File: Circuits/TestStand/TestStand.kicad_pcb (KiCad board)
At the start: 2 copper layers, 105 x 142.5 mm, 109 parts, among them IC1 STP85NF55, J1 2601-1107, J10 Screw_Terminal_01x03, J11 Screw_Terminal_01x03, J12 Screw_Terminal_01x03, J13 Screw_Terminal_01x03, J14 CONN4_2606-1104/010-000_WAG, J15 Conn_Coaxial, J18 2601-1107, J2 2601-1107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

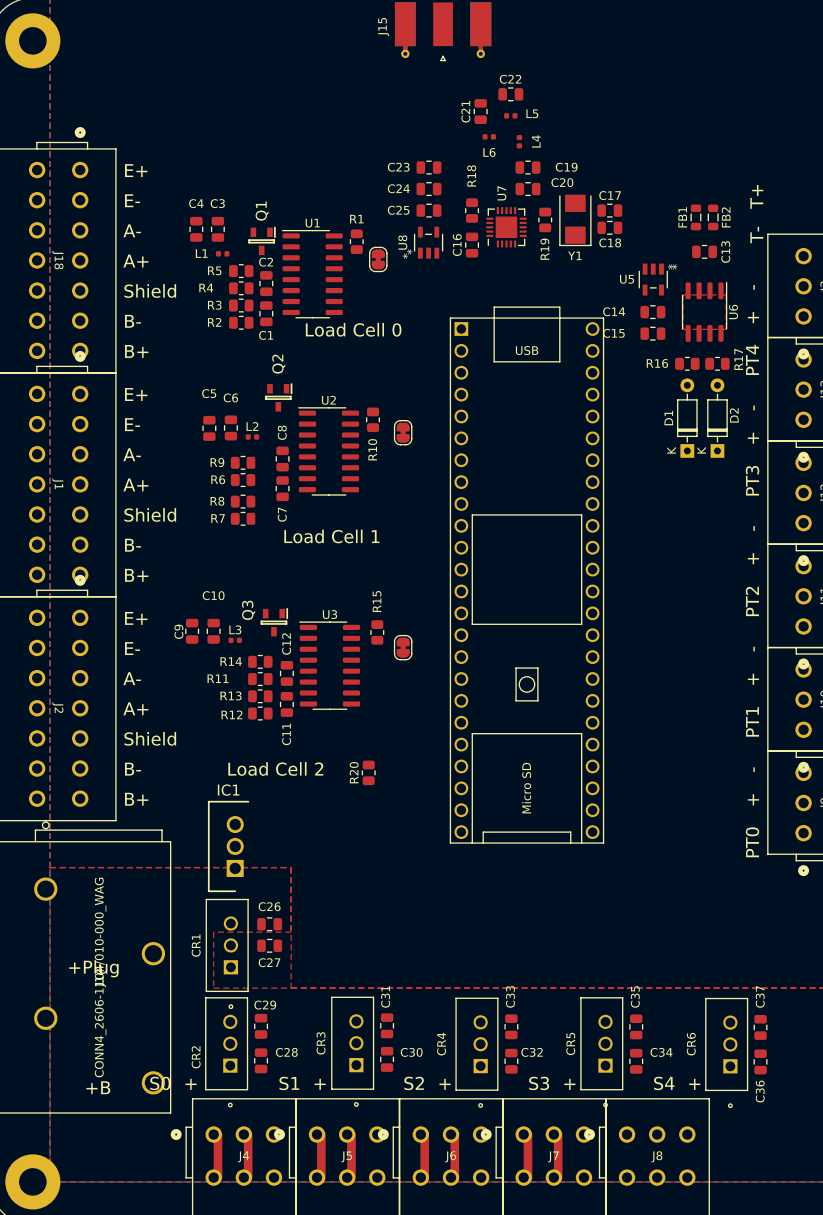
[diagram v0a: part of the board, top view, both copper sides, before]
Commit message: fixed 3d models, arranged nicely
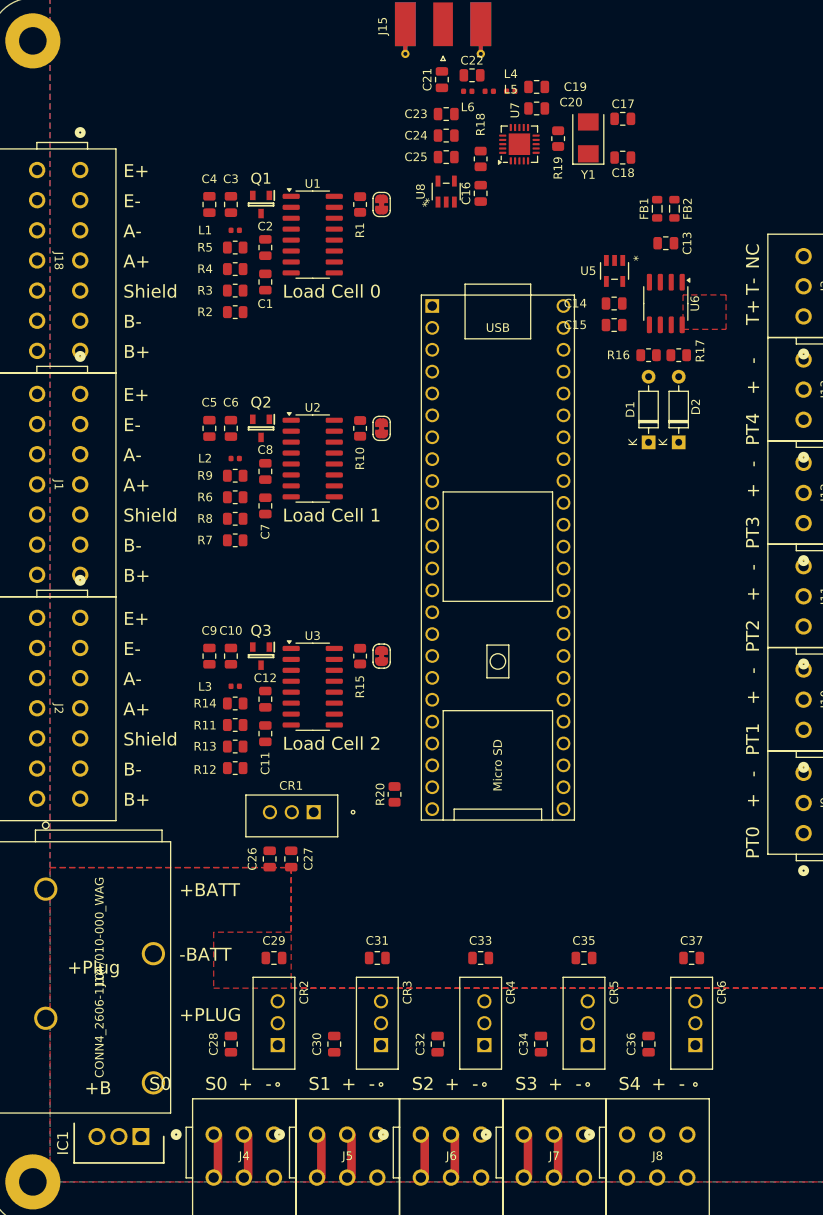
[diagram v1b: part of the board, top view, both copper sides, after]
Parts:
- moved IC1 33.0 mm to (33.0, 195.2), turned to 180 degrees
- moved CR1 20.4 mm to (53.1, 157.6), turned to 180 degrees
- moved C36 13.2 mm to (92.0, 184.5)
- moved C37 11.4 mm to (97.0, 174.5), turned to 0 degrees
- moved C34 11.2 mm to (79.5, 184.5)
- moved C17 10.8 mm to (89.0, 77.1)
- moved C27 10.4 mm to (50.5, 163.0), turned to -90 degrees
- moved C35 10.0 mm to (84.5, 174.5), turned to 0 degrees
- moved U7 9.76 mm to (77.0, 80.0)
- moved R19 9.56 mm to (81.5, 79.4)
- moved Y1 9.56 mm to (85.0, 79.3)
- moved C19 9.41 mm to (79.0, 73.4)
- moved C20 9.41 mm to (79.0, 75.9)
- moved C32 8.80 mm to (67.5, 184.5)
- moved C33 8.75 mm to (72.5, 174.5), turned to 0 degrees
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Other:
- board text added: "+BATT"
- board text added: "+PLUG"
- board text added: "-BATT"
- board text added: "NC"

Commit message: Some more silkscreen final touches GO TO BED
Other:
- board text added: "AD ASTRA PER IRAM"
- board text added: "LERT"

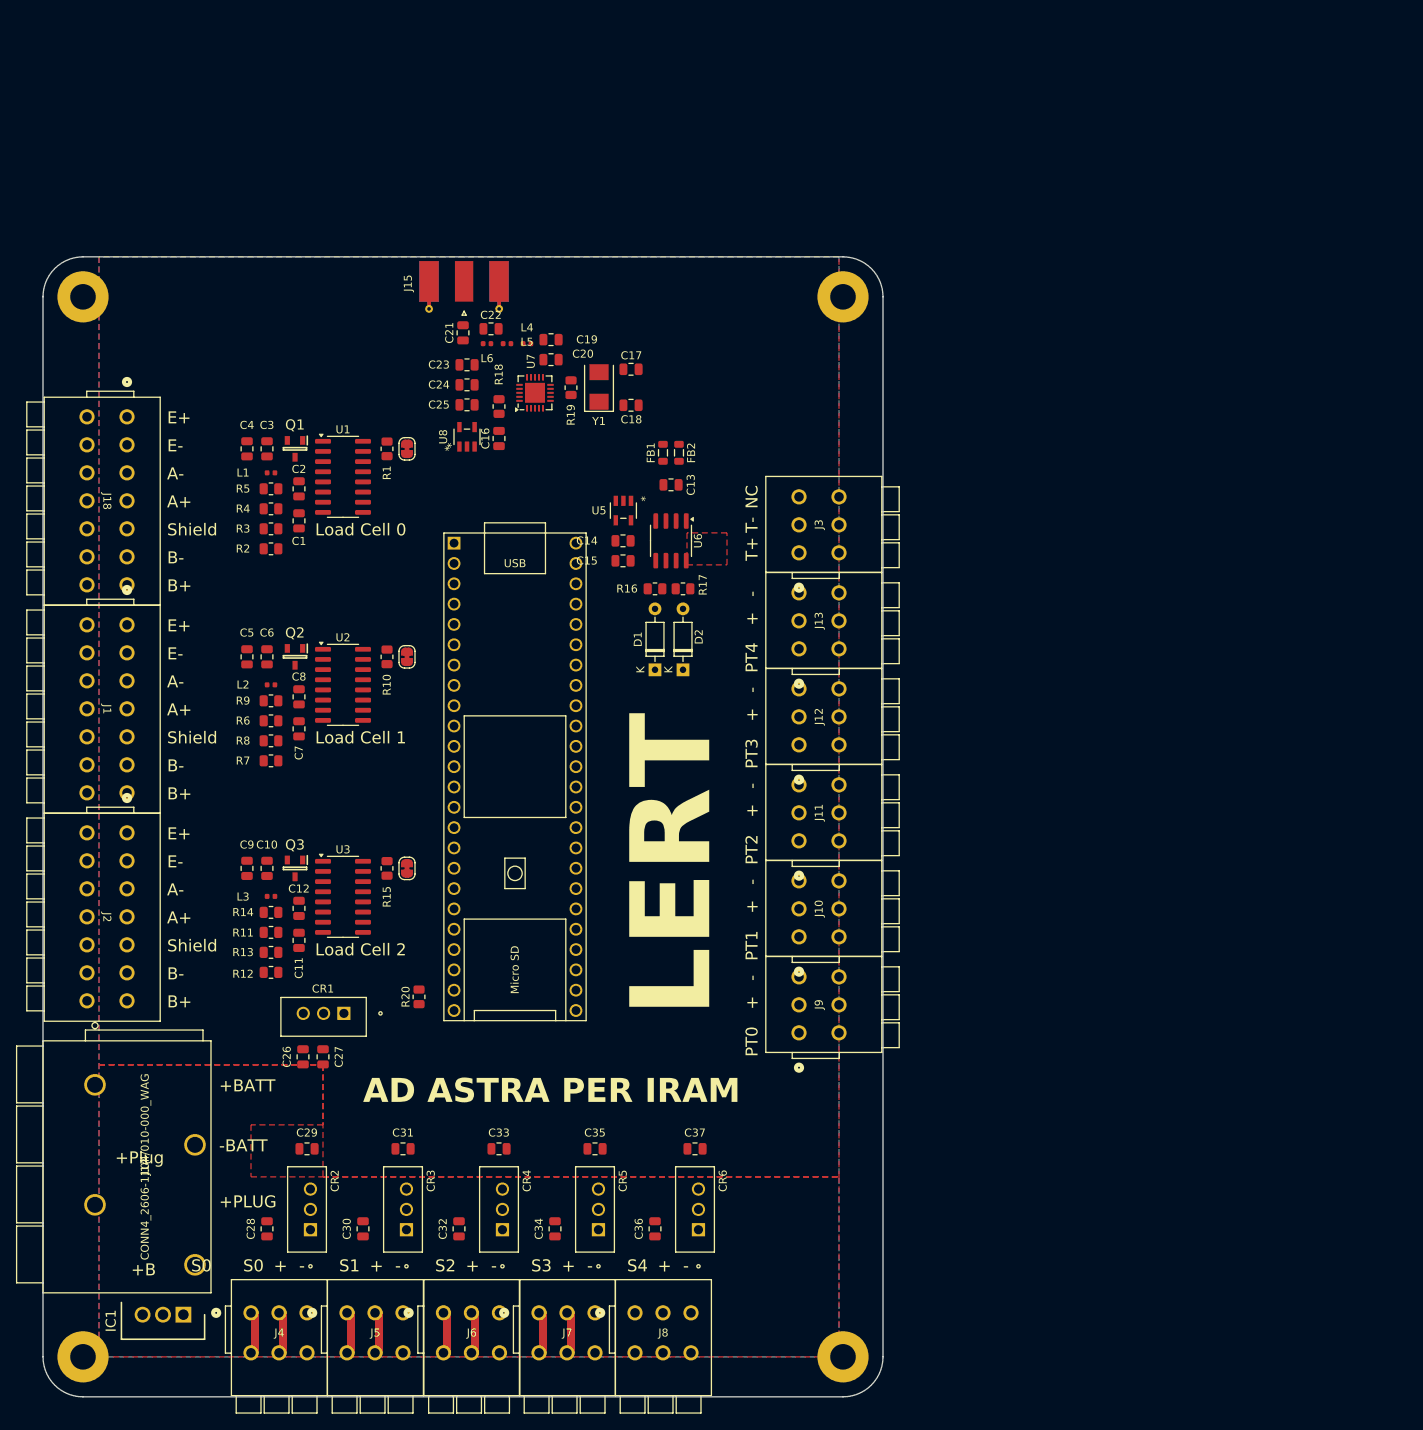
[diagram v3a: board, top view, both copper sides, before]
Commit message: added optoisolators and did some routing
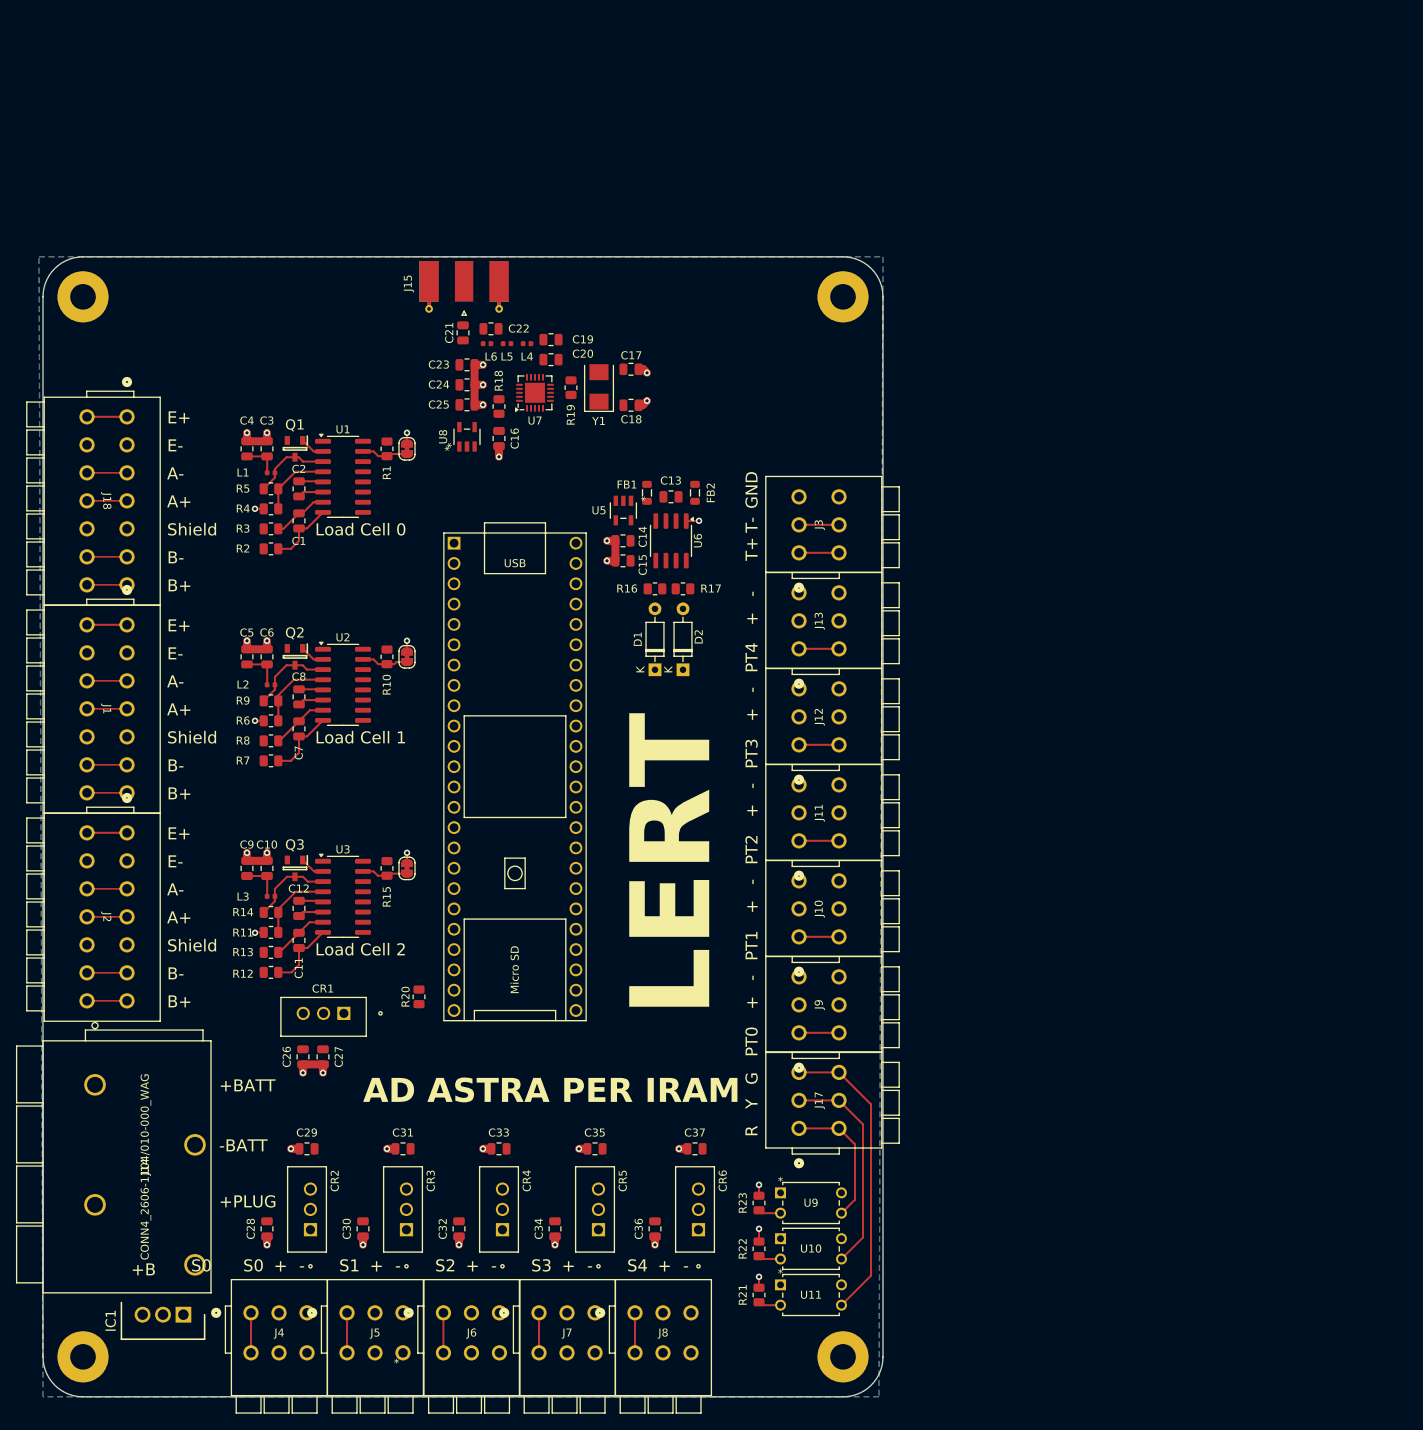
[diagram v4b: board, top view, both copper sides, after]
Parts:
- added J17: Screw_Terminal_01x03, Library:CONN3_2601-1103_WAG, F.Cu at (110.0, 171.9)
- added R21: 220, Resistor_SMD:R_0805_2012Metric, F.Cu at (105.0, 192.8)
- added R22: 220, Resistor_SMD:R_0805_2012Metric, F.Cu at (105.0, 187.0)
- added R23: 220, Resistor_SMD:R_0805_2012Metric, F.Cu at (105.0, 181.3)
- added U10: VO615A-X001, Library:DIP-4_VO615A_VIS, F.Cu at (107.7, 185.7)
- added U11: VO615A-X001, Library:DIP-4_VO615A_VIS, F.Cu at (107.7, 191.5)
- added U9: VO615A-X001, Library:DIP-4_VO615A_VIS, F.Cu at (107.7, 180.0)
- moved FB1 5.39 mm to (91.0, 92.5)
- moved FB2 5.39 mm to (97.0, 92.5)
- moved C13 1.50 mm to (94.0, 93.0)
- turned C26 to 90 degrees
- turned C27 to 90 degrees
- turned JP3 to -90 degrees
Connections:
- J3 pad 5: unconnected-(J3-3_1-Pad5) -> GND
- J3 pad 6: unconnected-(J3-3_2-Pad6) -> GND
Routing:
- net GND: track 0.00 -> 67.7 mm, vias 0 -> 36
- net /GREEN: track 0.00 -> 37.3 mm
- net /YELLOW: track 0.00 -> 27.2 mm
- net /RED: track 0.00 -> 17.1 mm
- net Net-(U2-AVDD): track 0.00 -> 10.4 mm
- net Net-(U3-AVDD): track 0.00 -> 10.4 mm
- net /E1+: track 0.00 -> 10.1 mm
- net /E2+: track 0.00 -> 10.1 mm
- net Net-(U1-AVDD): track 0.00 -> 9.91 mm
- net Net-(U2-VFB): track 0.00 -> 9.59 mm
- net /E+: track 0.00 -> 9.56 mm
- net Net-(U3-VFB): track 0.00 -> 9.39 mm
- net Net-(U1-VFB): track 0.00 -> 8.97 mm
- net Net-(U3-INA+): track 0.00 -> 8.89 mm
- net Net-(U2-INA+): track 0.00 -> 8.88 mm
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- removed copper zone on F.Cu, net +5V
- removed copper zone on F.Cu, net +BATT
- removed copper zone on F.Cu, net GND
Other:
- board text added: "G"
- board text added: "GND"
- board text added: "R"
- board text added: "Y"
- board text removed: "+Plug"
- board text removed: "NC"

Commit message: ALMOST DOWN ROUTING
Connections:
- U4 pad 43: unconnected-(U4-21_A7_RX5_BCLK1-Pad43) -> /GPIN
- U4 pad 44: unconnected-(U4-22_A8_CTX1-Pad44) -> /YPIN
- U4 pad 45: unconnected-(U4-23_A9_CRX1_MCLK1-Pad45) -> /RPIN
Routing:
- net +5V: track 0.00 -> 100.6 mm, vias 0 -> 2
- net /GPIN: track 0.00 -> 96.9 mm, vias 0 -> 2
- net /PWM0: track 5.00 -> 96.5 mm
- net /GP: track 0.00 -> 90.4 mm, vias 0 -> 1
- net /YPIN: track 0.00 -> 89.4 mm, vias 0 -> 2
- net /PWM4: track 5.00 -> 92.5 mm
- net /RPIN: track 0.00 -> 87.5 mm, vias 0 -> 2
- net /PWM1: track 5.00 -> 89.1 mm
- net /PWM3: track 5.00 -> 83.8 mm
- net /PWM2: track 5.00 -> 82.3 mm
- net /rIRQ: track 0.00 -> 74.5 mm, vias 0 -> 1
- net /rCE: track 0.00 -> 68.9 mm
- net /rSCK: track 0.00 -> 66.8 mm, vias 0 -> 1
- net /rCSN: track 0.00 -> 66.1 mm
- net /rMOSI: track 0.00 -> 64.4 mm, vias 0 -> 1
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- added copper zone on F.Cu, net +5V
- added copper zone on F.Cu, net +BATT

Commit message: basically done
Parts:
- moved CR4 70.2 mm to (136.4, 154.6)
- moved CR5 70.2 mm to (148.4, 154.6)
- moved CR6 70.2 mm to (160.9, 154.6)
- moved J15 70.2 mm to (131.6, 37.7)
- moved J6 70.2 mm to (129.0, 164.9)
- moved U5 70.2 mm to (151.5, 64.7)
- moved C1 70.2 mm to (110.9, 65.9)
- moved C10 70.2 mm to (106.9, 109.4)
- moved C11 70.2 mm to (110.9, 118.4)
- moved C12 70.2 mm to (110.9, 114.4)
- moved C13 70.2 mm to (157.4, 62.9)
- moved C14 70.2 mm to (151.4, 68.4)
- moved C15 70.2 mm to (151.4, 70.9)
- moved C16 70.2 mm to (135.9, 55.7)
- moved C17 70.2 mm to (152.4, 47.0)
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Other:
- board text added: "V0.1 PCB By Isaac Sal"
